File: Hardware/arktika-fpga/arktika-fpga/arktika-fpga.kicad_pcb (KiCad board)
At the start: 4 copper layers, 133.2 x 81.3 mm, 135 parts

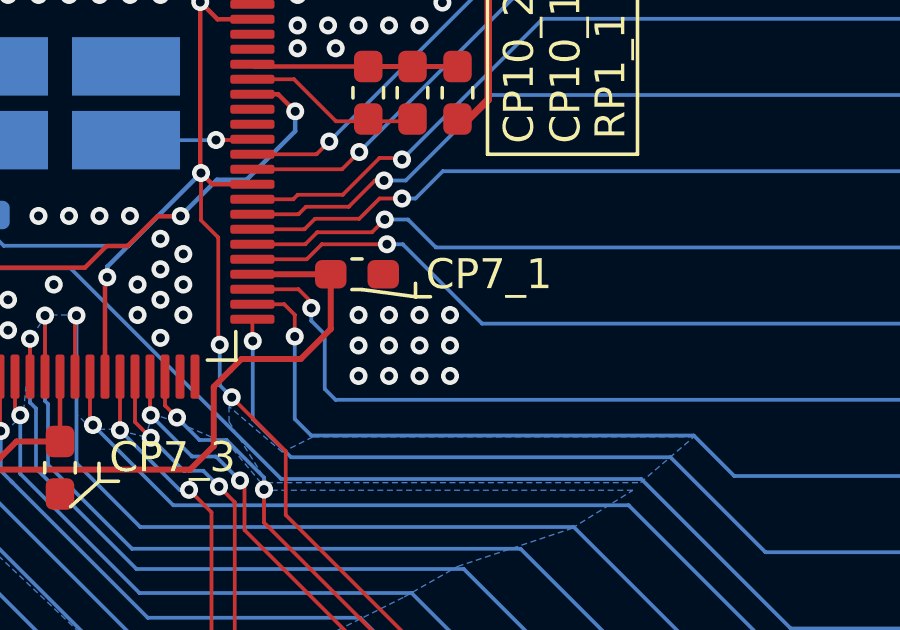
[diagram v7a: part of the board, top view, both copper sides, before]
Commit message: Fixed minor drc errors. removed usb jumpers and added needed resistors
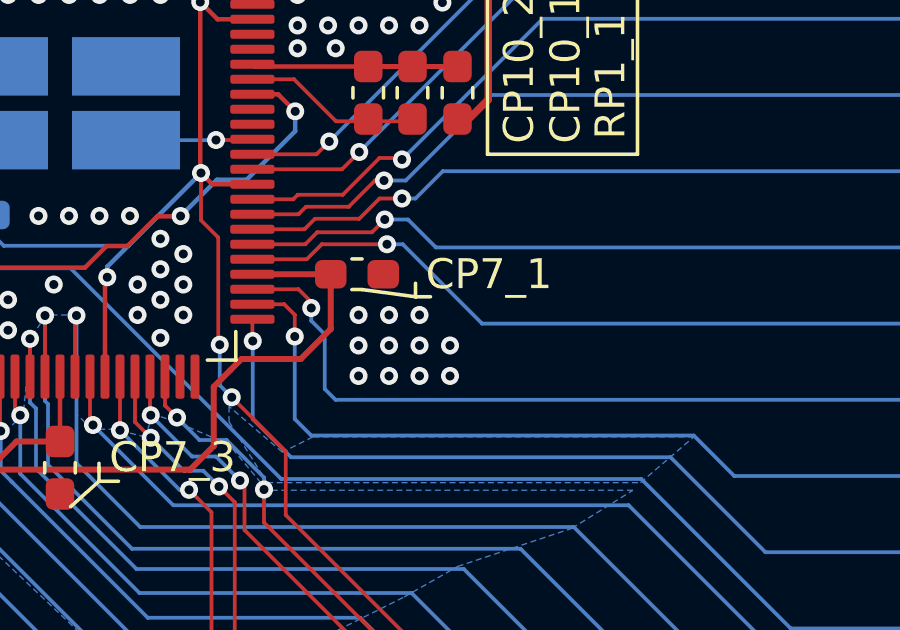
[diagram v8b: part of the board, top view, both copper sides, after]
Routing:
- net GND: vias 237 -> 236
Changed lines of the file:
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@@
     (thickness 1.6002)
     (drawings 300)
-    (tracks 2618)
+    (tracks 2617)
     (zones 0)
     (modules 135)
@@
   (via (at 188.468 102.108) (size 0.6) (drill 0.3) (layers Front Back) (net 11))
   (via (at 189.484 102.108) (size 0.6) (drill 0.3) (layers Front Back) (net 11))
-  (via (at 190.5 102.108) (size 0.6) (drill 0.3) (layers Front Back) (net 11))
   (via (at 185.42 91.44) (size 0.6) (drill 0.3) (layers Front Back) (net 11))
   (via (at 185.42 92.456) (size 0.6) (drill 0.3) (layers Front Back) (net 11))
